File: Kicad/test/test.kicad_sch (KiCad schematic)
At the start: 12 parts, among them J2 PrgmUART, U2 ESP32-S3-WROOM-1

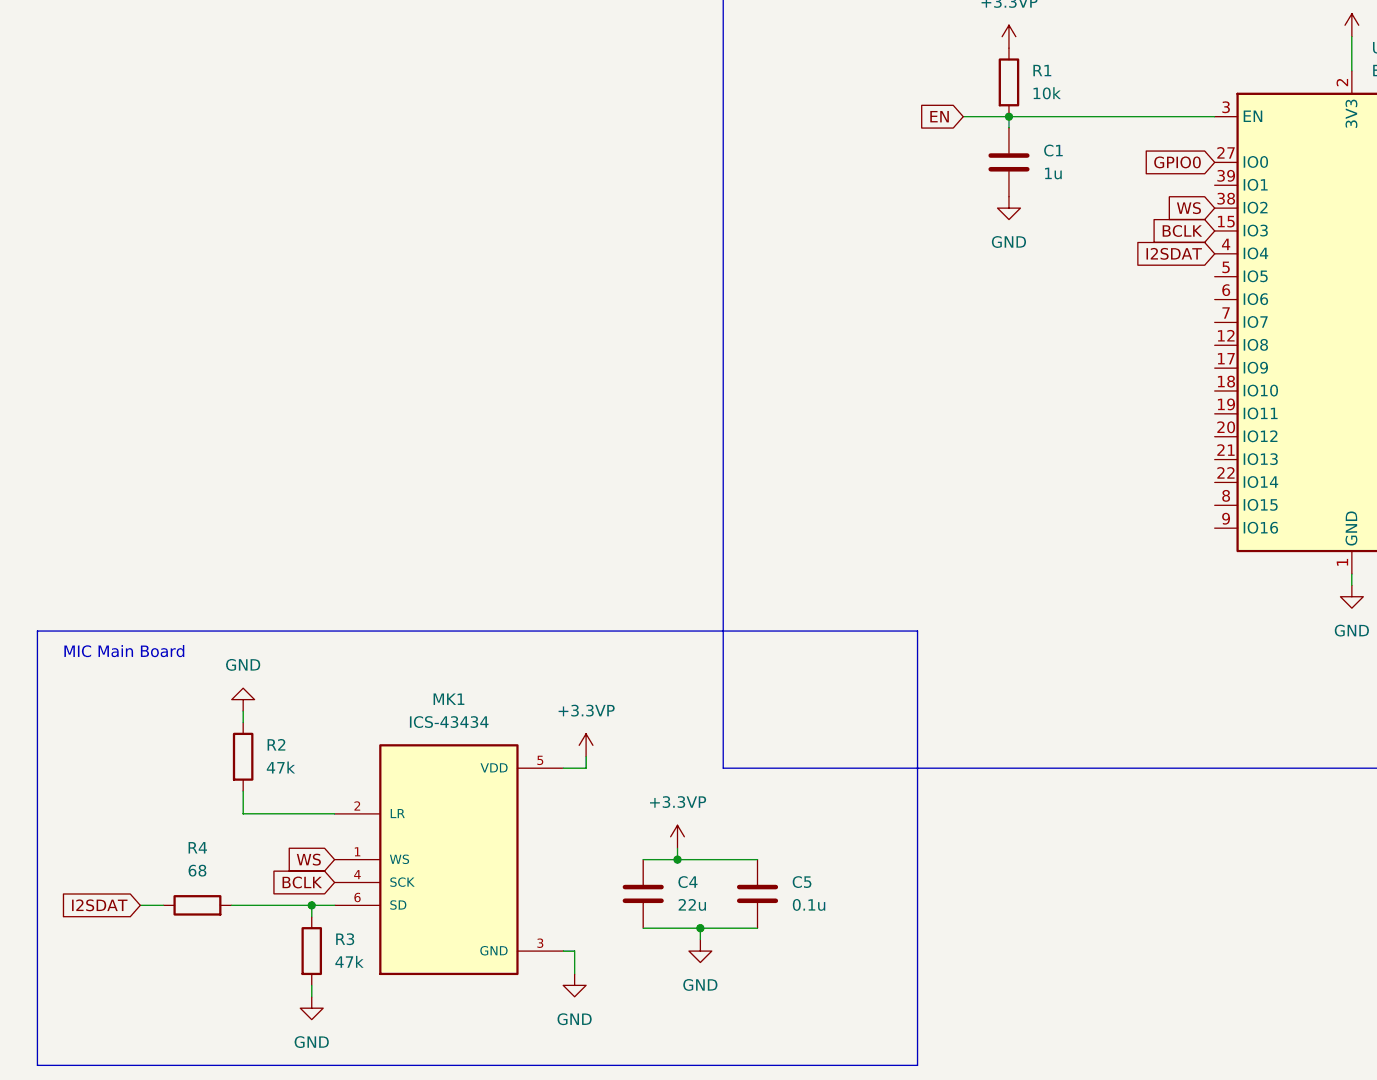
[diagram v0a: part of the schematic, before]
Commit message: Implemented Amplifier
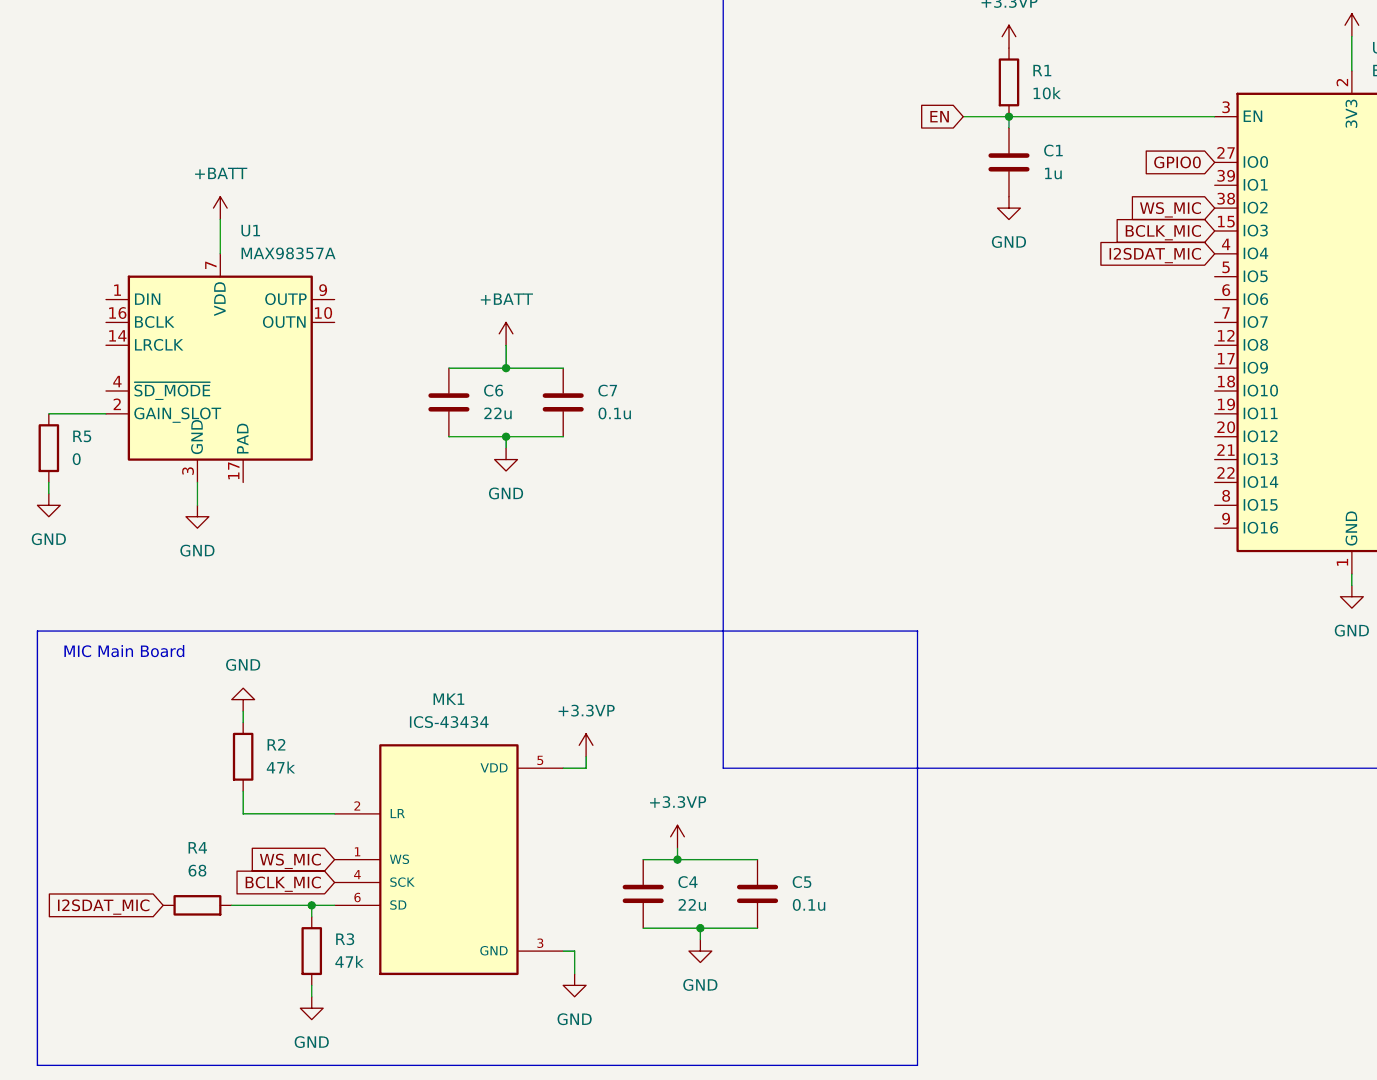
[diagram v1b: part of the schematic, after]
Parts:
- added C6: 22u, symbol Device:C
- added C7: 0.1u, symbol Device:C
- added R5: 0, symbol Device:R
- added U1: MAX98357A, Package_DFN_QFN:TQFN-16-1EP_3x3mm_P0.5mm_EP1.23x1.23mm, symbol Audio:MAX98357A
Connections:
- net GND: now also C6.2, C7.2, R5.2, U1.11 (GND), U1.15 (GND), U1.3 (GND)
- net BCLK renamed BCLK_MIC
- net I2SDAT renamed I2SDAT_MIC
- net WS renamed WS_MIC
- new net: R5.1, U1.2 (GAIN_SLOT)
- new net +BATT: C6.1, C7.1, U1.7 (VDD), U1.8 (VDD)

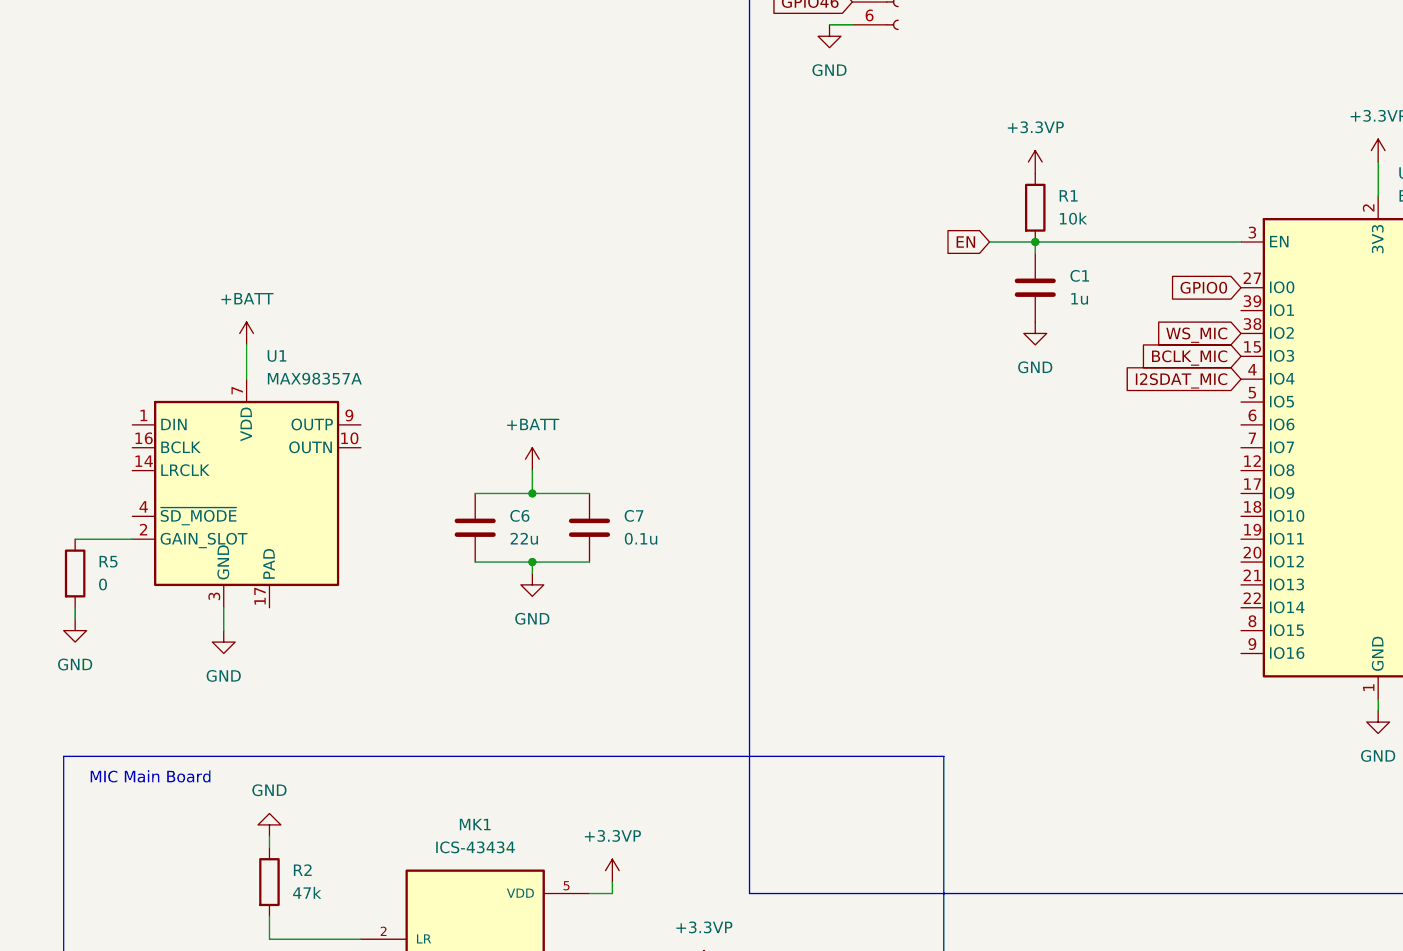
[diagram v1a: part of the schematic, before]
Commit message: Implemented Amplifier
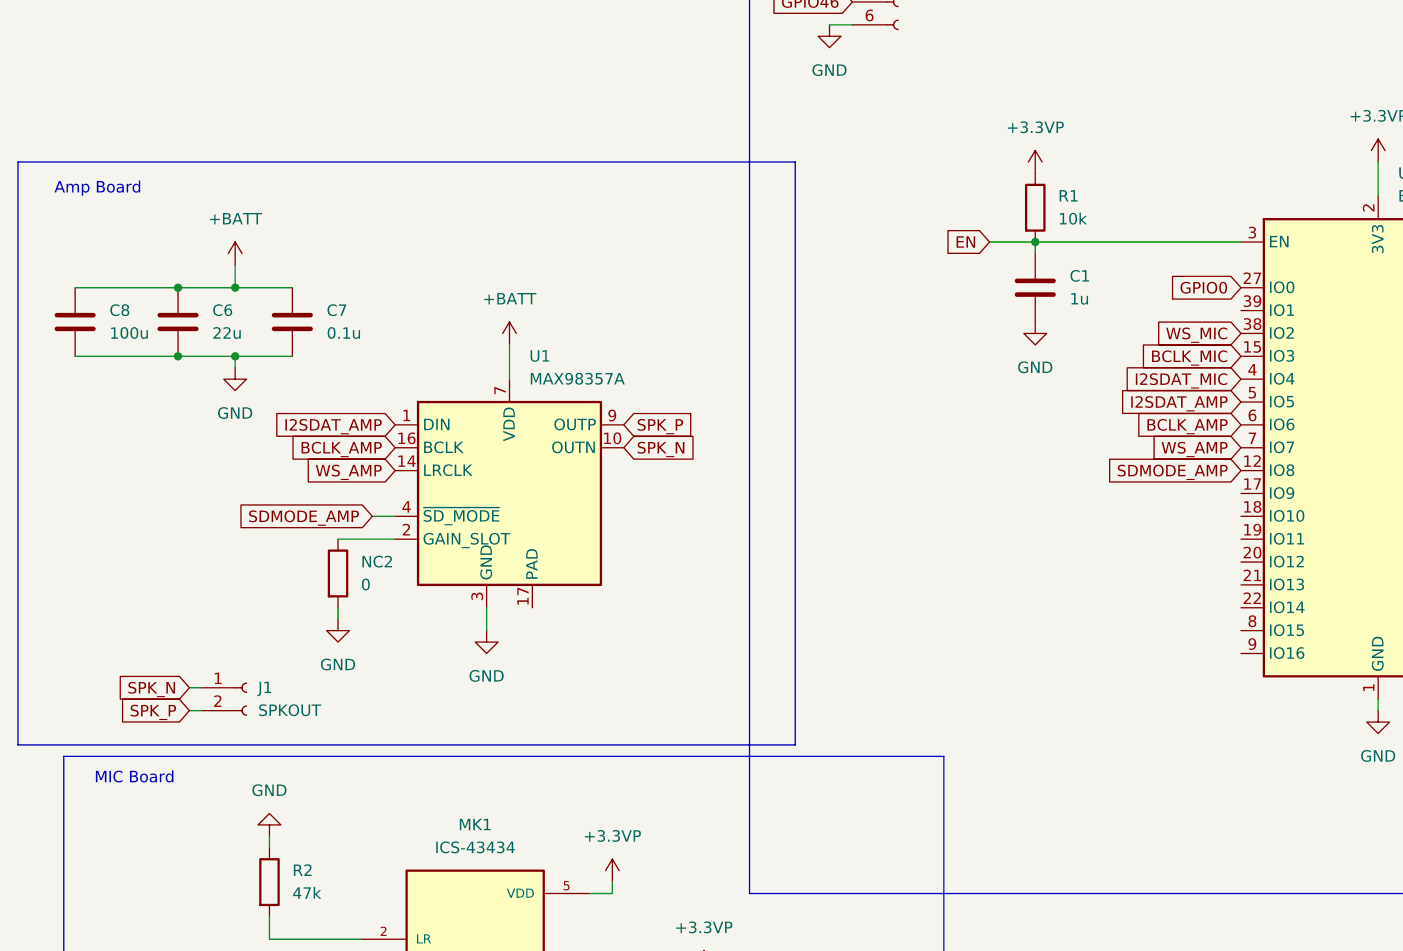
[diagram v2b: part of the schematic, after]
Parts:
- added C8: 100u, symbol Device:C
- added J1: SPKOUT, symbol Connector:Conn_01x02_Socket
- renumbered R5 to NC2
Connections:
- net +BATT: now also C8.1
- net GND: now also C8.2
- net I2SDAT_AMP: now reaches U1.1 (DIN)
- net I2SDAT_AMP: now also U2.5 (IO5)
- net SPK_N: now reaches U1.10 (OUTN)
- net SPK_N: now also J1.1 (Pin_1)
- net WS_AMP: now reaches U1.14 (LRCLK)
- net WS_AMP: now also U2.7 (IO7)
- net BCLK_AMP: now reaches U1.16 (BCLK)
- net BCLK_AMP: now also U2.6 (IO6)
- net SDMODE_AMP: now reaches U1.4 (~{SD_MODE})
- net SDMODE_AMP: now also U2.12 (IO8)
- net SPK_P: now reaches U1.9 (OUTP)
- net SPK_P: now also J1.2 (Pin_2)
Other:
- note added: "Amp Board"
- note added: "MIC Board"
- note removed: "MIC Main Board"
- moved on the sheet: C6, C7, NC2, U1

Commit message: Implemented ov5640
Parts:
- added C10, C11, C12, C13: 100n, symbol Device:C
- added C9: 15p, symbol Device:C
- added NC1, NC3: 0, symbol Device:R
- added R5, R6, R7: 4.7k, symbol Device:R
- added U3: ~, symbol ov5640:OV5640
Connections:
- net GND: now also C10.2, C11.2, C12.2, C13.2, C9.2, NC1.2, U3.15 (DGND), U3.2 (AGND)
- net +3.3VP renamed +3V3
- net +3V3: now also C10.1, R5.2, R6.2, R7.2, U3.11 (DOVDD)
- new net: C13.1, NC3.1, R7.1
- new net +1V5: U3.10 (DVDD)
- new net +2V8: C11.1, C12.1, U3.4 (AVDD)
- new net CAM_HREF: U3.9 (HREF)
- new net CAM_MCLK: U3.13 (MCLK)
- new net CAM_PCLK: C9.1, U3.17 (PCLK)
- new net CAM_PWDN: NC1.1, U3.8 (PWDN)
- new net CAM_RESET: NC3.2, U3.6 (RESET)
- new net CAM_SCL: R6.1, U3.5 (SCL)
- new net CAM_SDA: R5.1, U3.3 (SDA)
- new net CAM_VSYNC: U3.7 (VSYNC)
- new net CAM_Y2: U3.19 (Y2)
- new net CAM_Y3: U3.21 (Y3)
- new net CAM_Y4: U3.22 (Y4)
- new net CAM_Y5: U3.20 (Y5)
- new net CAM_Y6: U3.18 (Y6)
- new net CAM_Y7: U3.16 (Y7)
- new net CAM_Y8: U3.14 (Y8)
- new net CAM_Y9: U3.12 (Y9)
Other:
- note added: "CAM Board"

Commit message: Schematic finished
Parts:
- added C14, C24: 1u, symbol Device:C
- added C15, C18, C20, C21, C23, C25, C26: 10u, symbol Device:C
- added C16, C17, C19, C22: 22u, symbol Device:C
- added C27, C28, C29, C30: 100n, symbol Device:C
- added D1: LED, symbol Device:LED
- added D2, D4: WS2812B, LED_SMD:LED_WS2812B_PLCC4_5.0x5.0mm_P3.2mm, symbol LED:WS2812B
- added J3: USB_C_Receptacle_PowerOnly_6P, symbol Connector:USB_C_Receptacle_PowerOnly_6P
- added L1, L2: 1u, symbol Device:L
- added NC4: 0, symbol Device:R
- added R10, R8, R9: 4.7k, symbol Device:R
- added R11: 1k, symbol Device:R
- added R12, R13, R14, R15: 10k, symbol Device:R
- added SW1, SW2, SW3, SW4, SW5: SW_Push, symbol Switch:SW_Push
- added U5: ~, symbol pmic:AXP2101
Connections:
- net +1V5: now also U5.18 (ALDO1)
- net +2V8: now also U5.19 (ALDO2)
- net +3V3: now also C19.2, L1.2, R10.2, R12.1, R13.1, R14.1, R15.1, R8.2, R9.2, U5.21 (FB1); no longer C10.1, R5.2, R6.2, R7.2, U3.11 (DOVDD)
- net CAM_HREF: now also U2.13 (IO19)
- net CAM_MCLK: now also U2.23 (IO21)
- net CAM_PCLK: now also U2.21 (IO13)
- net CAM_PWDN: now also U2.18 (IO10)
- net CAM_RESET: now also U2.17 (IO9)
- net CAM_SCL: now also U2.10 (IO17)
- net CAM_SDA: now also U2.11 (IO18)
- net CAM_VSYNC: now also U2.14 (IO20)
- net CAM_Y2: now also U2.26 (IO45)
- net CAM_Y3: now also U2.35 (IO42)
- net CAM_Y4: now also U2.34 (IO41)
- net CAM_Y5: now also U2.33 (IO40)
- net CAM_Y6: now also U2.32 (IO39)
- net CAM_Y7: now also U2.31 (IO38)
- net CAM_Y8: now also U2.19 (IO11)
- net CAM_Y9: now also U2.20 (IO12)
- net EN: now also SW1.2
- net GND: now also C14.1, C15.1, C16.1, C17.1, C18.1, C19.1, C20.2, C21.1, C22.1, C23.1, C24.1, C25.1, C26.1, C27.2, C28.2, C29.2, C30.2, D2.3 (VSS), D4.3 (VSS), J3.A12 (GND), J3.B12 (GND), J3.S1 (SHIELD), SW1.1, SW2.1, SW3.1, SW4.1, SW5.1, U5.3 (GND), U5.41 (EP)
- net PMIC_SCL: now reaches U2.22 (IO14)
- net PMIC_SCL: now also R8.1, U5.40 (SCK)
- net SW_L3: now reaches U2.24 (IO47)
- net SW_L3: now also C27.1, R12.2, SW3.2
- net PMIC_PWROK: now reaches U2.28 (IO35)
- net PMIC_PWROK: now also U5.29 (PWROK)
- net SW_L1: now reaches U2.29 (IO36)
- net SW_L1: now also C30.1, R15.2, SW5.2
- net SW_L2: now reaches U2.30 (IO37)
- net SW_L2: now also C29.1, R14.2, SW2.2
- net LEDCNTRL: now reaches U2.39 (IO1)
- net LEDCNTRL: now also D4.4 (DIN)
- net PMIC_SDA: now reaches U2.8 (IO15)
- net PMIC_SDA: now also R9.1, U5.39 (SDA)
- net PMIC_IRQ: now reaches U2.9 (IO16)
- net PMIC_IRQ: now also R10.1, U5.38 (IRQ)
- net +BATT renamed VSYS
- net VSYS: now also C16.2, C17.2, C18.2, C20.1, C21.2, C25.2, C26.2, D2.1 (VDD), D4.1 (VDD), R11.2, U5.17 (ALDOIN), U5.23 (VIN1), U5.24 (VIN2), U5.34 (VSYS), U5.36 (VMID)
- new net: D2.4 (DIN), D4.2 (DOUT)
- new net: C14.2, U5.2 (VREF)
- new net: C28.1, NC4.1, R13.2, SW4.2
- new net: D1.2 (A), R11.1
- new net: L2.1, U5.25 (LX2)
- new net: D1.1 (K), U5.1 (CHGLED)
- new net: L1.1, U5.22 (LX1)
- new net PMIC_PWRON: NC4.2, U5.30 (PWRON)
- new net VBAT: U5.33 (BAT)
- new net VBUS: C15.2, J3.A9 (VBUS), J3.B9 (VBUS), U5.37 (VBUS)
- new net VCAM3V3: C10.1, C22.2, C23.2, C24.2, L2.2, R5.2, R6.2, R7.2, U3.11 (DOVDD), U5.26 (FB2)
- no-connect marks 0 -> 24
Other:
- note added: "Color LED Board"
- note added: "PMIC Board"
- note added: "Switch Board"
